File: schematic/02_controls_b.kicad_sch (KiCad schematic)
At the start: 19 parts, among them SW107 F sharp, SW108 G, SW109 G sharp, SW110 A, SW111 A sharp, SW112 B, U402 74HC14

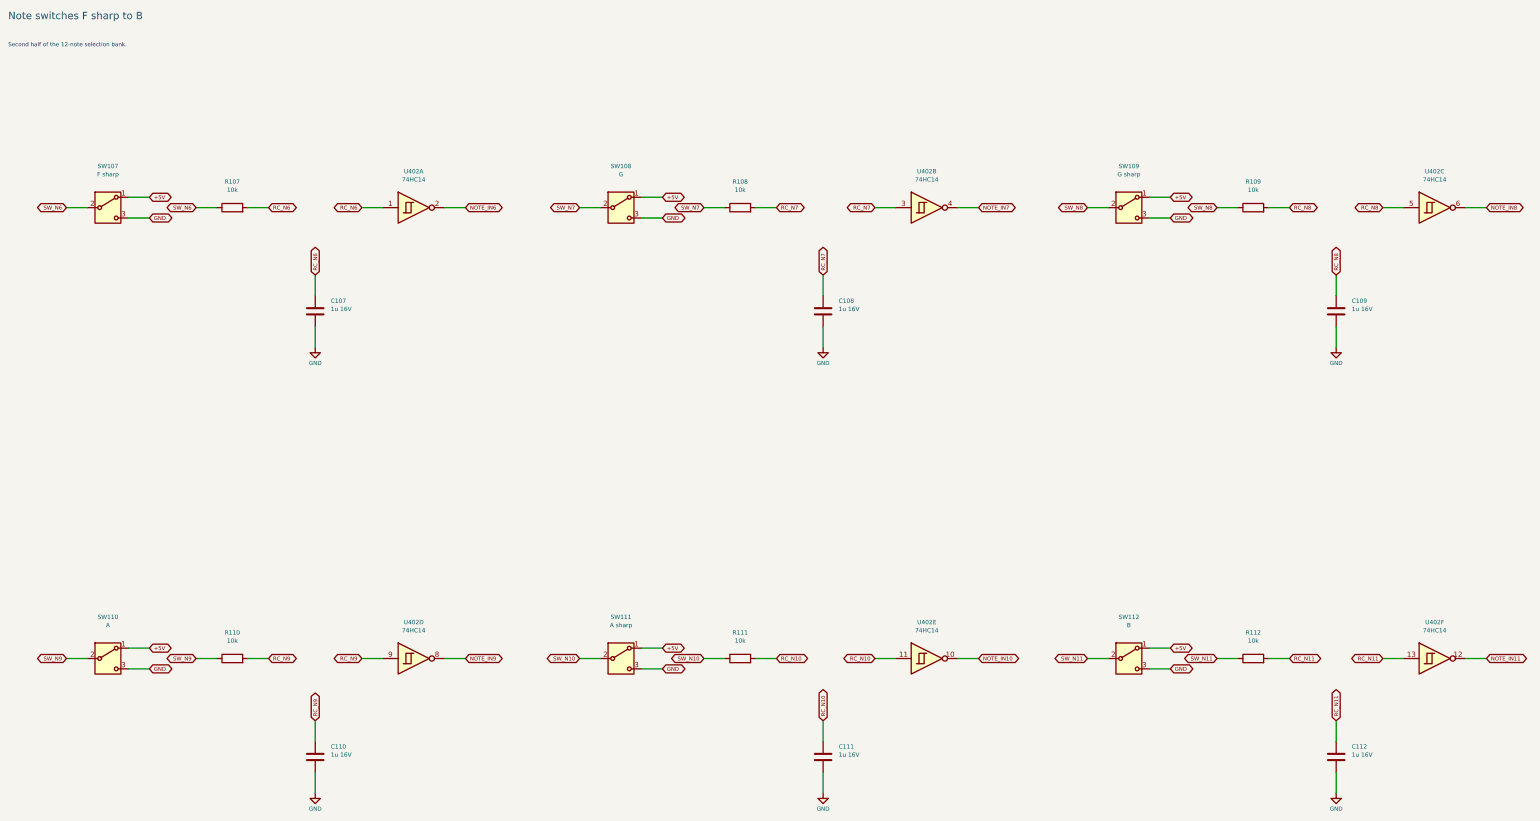
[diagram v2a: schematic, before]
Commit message: pick controls and start pcb placement
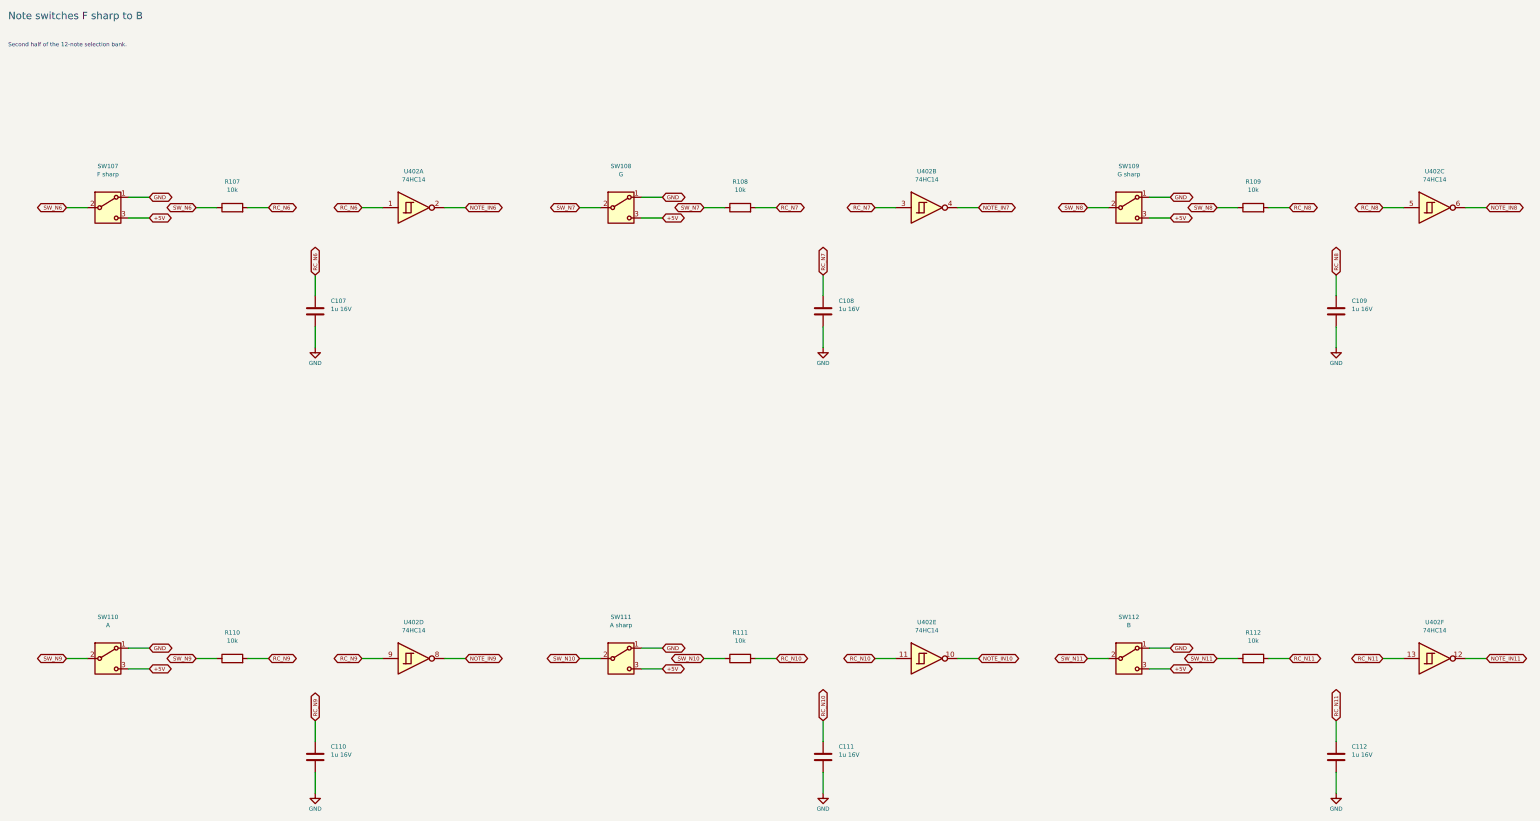
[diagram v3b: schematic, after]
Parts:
- SW107, SW108, SW109, SW110, SW111, SW112: footprint (none) -> Arpeggiator:SW_Dailywell_1M_SPDT_M2; MPN (none) -> 1MS1T1B1M2QES; Manufacturer (none) -> Dailywell; Supplier (none) -> Tayda; Supplier URL (none) -> https://www.taydaelectronics.com/electromechanical/switches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
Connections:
- net +5V: now also SW107.3 (C), SW108.3 (C), SW109.3 (C), SW110.3 (C), SW111.3 (C), SW112.3 (C); no longer SW107.1 (A), SW108.1 (A), SW109.1 (A), SW110.1 (A), SW111.1 (A), SW112.1 (A)
- net GND: now also SW107.1 (A), SW108.1 (A), SW109.1 (A), SW110.1 (A), SW111.1 (A), SW112.1 (A); no longer SW107.3 (C), SW108.3 (C), SW109.3 (C), SW110.3 (C), SW111.3 (C), SW112.3 (C)
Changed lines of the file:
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@@
       )
     )
-    (property "Footprint" ""
+    (property "Footprint" "Arpeggiator:SW_Dailywell_1M_SPDT_M2"
       (at 44.45 54.61 0.0)
       (effects
@@
       )
     )
-    (property "Datasheet" ""
+    (property "Datasheet" "https://www.taydaelectronics.com/datasheets/files/1M_series.pdf"
       (at 44.45 54.61 0.0)
       (effects
         (font
           (size 1.05 1.05)
+        )
+        (hide yes)
+      )
+    )
+    (property "MPN" "1MS1T1B1M2QES"
+      (at 44.45 64.77 0.0)
+      (effects
+        (font
+          (size 1.0 1.0)
+        )
+        (hide yes)
+      )
+    )
+    (property "Manufacturer" "Dailywell"
+      (at 44.45 64.77 0.0)
+      (effects
+        (font
+          (size 1.0 1.0)
+        )
+        (hide yes)
+      )
+    )
+    (property "Supplier" "Tayda"
+      (at 44.45 64.77 0.0)
+      (effects
+        (font
+          (size 1.0 1.0)
+        )
+        (hide yes)
+      )
+    )
+    (property "Supplier URL" "https://www.taydaelectronics.com/electromechanical/switches-key-pad/toggle-switch/mini-toggle-switch-spdt-on-none-on-pc-thru-hole.html"
+      (at 44.45 64.77 0.0)
+      (effects
+        (font
+          (size 1.0 1.0)
         )
         (hide yes)
@@
     )
   )
-  (global_label "+5V"
+  (global_label "GND"
     (shape bidirectional)
     (at 54.61 62.23 0.0)
@@
     )
   )
-  (global_label "GND"
+  (global_label "+5V"
     (shape bidirectional)
     (at 54.61 67.31 0.0)
@@
       )
     )
-    (property "Footprint" ""
+    (property "Footprint" "Arpeggiator:SW_Dailywell_1M_SPDT_M2"
       (at 170.18 54.61 0.0)
       (effects
@@
       )
     )
-    (property "Datasheet" ""
+    (property "Datasheet" "https://www.taydaelectronics.com/datasheets/files/1M_series.pdf"
       (at 170.18 54.61 0.0)
       (effects
         (font
           (size 1.05 1.05)
+        )
+        (hide yes)
+      )
+    )
+    (property "MPN" "1MS1T1B1M2QES"
+      (at 170.18 64.77 0.0)
+      (effects
+        (font
+          (size 1.0 1.0)
+        )
+        (hide yes)
+      )
+    )
+    (property "Manufacturer" "Dailywell"
+      (at 170.18 64.77 0.0)
+      (effects
+        (font
+          (size 1.0 1.0)
+        )
+        (hide yes)
+      )
+    )
+    (property "Supplier" "Tayda"
+      (at 170.18 64.77 0.0)
+      (effects
+        (font
+          (size 1.0 1.0)
+        )
+        (hide yes)
+      )
+    )
+    (property "Supplier URL" "https://www.taydaelectronics.com/electromechanical/switches-key-pad/toggle-switch/mini-toggle-switch-spdt-on-none-on-pc-thru-hole.html"
+      (at 170.18 64.77 0.0)
+      (effects
+        (font
+          (size 1.0 1.0)
         )
         (hide yes)
@@
     )
   )
-  (global_label "+5V"
+  (global_label "GND"
     (shape bidirectional)
     (at 180.34 62.23 0.0)
@@
     )
   )
-  (global_label "GND"
+  (global_label "+5V"
     (shape bidirectional)
     (at 180.34 67.31 0.0)
@@
       )
     )
-    (property "Footprint" ""
+    (property "Footprint" "Arpeggiator:SW_Dailywell_1M_SPDT_M2"
       (at 294.64 54.61 0.0)
       (effects
@@
       )
     )
-    (property "Datasheet" ""
+    (property "Datasheet" "https://www.taydaelectronics.com/datasheets/files/1M_series.pdf"
       (at 294.64 54.61 0.0)
       (effects
         (font
           (size 1.05 1.05)
+        )
+        (hide yes)
+      )
+    )
+    (property "MPN" "1MS1T1B1M2QES"
+      (at 294.64 64.77 0.0)
+      (effects
+        (font
+          (size 1.0 1.0)
+        )
+        (hide yes)
+      )
+    )
+    (property "Manufacturer" "Dailywell"
+      (at 294.64 64.77 0.0)
+      (effects
+        (font
+          (size 1.0 1.0)
+        )
+        (hide yes)
+      )
+    )
+    (property "Supplier" "Tayda"
+      (at 294.64 64.77 0.0)
+      (effects
+        (font
+          (size 1.0 1.0)
+        )
+        (hide yes)
+      )
+    )
+    (property "Supplier URL" "https://www.taydaelectronics.com/electromechanical/switches-key-pad/toggle-switch/mini-toggle-switch-spdt-on-none-on-pc-thru-hole.html"
+      (at 294.64 64.77 0.0)
+      (effects
+        (font
+          (size 1.0 1.0)
         )
         (hide yes)
@@
     )
   )
-  (global_label "+5V"
+  (global_label "GND"
     (shape bidirectional)
     (at 304.8 62.23 0.0)
@@
     )
   )
-  (global_label "GND"
+  (global_label "+5V"
     (shape bidirectional)
     (at 304.8 67.31 0.0)
@@
       )
     )
-    (property "Footprint" ""
+    (property "Footprint" "Arpeggiator:SW_Dailywell_1M_SPDT_M2"
       (at 44.45 165.1 0.0)
       (effects
@@
       )
     )
-    (property "Datasheet" ""
+    (property "Datasheet" "https://www.taydaelectronics.com/datasheets/files/1M_series.pdf"
       (at 44.45 165.1 0.0)
       (effects
         (font
           (size 1.05 1.05)
+        )
+        (hide yes)
+      )
+    )
+    (property "MPN" "1MS1T1B1M2QES"
+      (at 44.45 175.26 0.0)
+      (effects
+        (font
+          (size 1.0 1.0)
+        )
+        (hide yes)
+      )
+    )
+    (property "Manufacturer" "Dailywell"
+      (at 44.45 175.26 0.0)
+      (effects
+        (font
+          (size 1.0 1.0)
+        )
+        (hide yes)
+      )
+    )
+    (property "Supplier" "Tayda"
+      (at 44.45 175.26 0.0)
+      (effects
+        (font
+          (size 1.0 1.0)
+        )
+        (hide yes)
+      )
+    )
+    (property "Supplier URL" "https://www.taydaelectronics.com/electromechanical/switches-key-pad/toggle-switch/mini-toggle-switch-spdt-on-none-on-pc-thru-hole.html"
+      (at 44.45 175.26 0.0)
+      (effects
+        (font
+          (size 1.0 1.0)
         )
         (hide yes)
@@
     )
   )
-  (global_label "+5V"
+  (global_label "GND"
     (shape bidirectional)
     (at 54.61 172.72 0.0)
@@
     )
   )
-  (global_label "GND"
+  (global_label "+5V"
     (shape bidirectional)
     (at 54.61 177.8 0.0)
@@
       )
     )
-    (property "Footprint" ""
+    (property "Footprint" "Arpeggiator:SW_Dailywell_1M_SPDT_M2"
       (at 170.18 165.1 0.0)
       (effects
@@
       )
     )
-    (property "Datasheet" ""
+    (property "Datasheet" "https://www.taydaelectronics.com/datasheets/files/1M_series.pdf"
       (at 170.18 165.1 0.0)
       (effects
         (font
           (size 1.05 1.05)
+        )
+        (hide yes)
+      )
+    )
+    (property "MPN" "1MS1T1B1M2QES"
+      (at 170.18 175.26 0.0)
+      (effects
+        (font
+          (size 1.0 1.0)
+        )
+        (hide yes)
+      )
+    )
+    (property "Manufacturer" "Dailywell"
+      (at 170.18 175.26 0.0)
+      (effects
+        (font
+          (size 1.0 1.0)
+        )
+        (hide yes)
+      )
+    )
+    (property "Supplier" "Tayda"
+      (at 170.18 175.26 0.0)
+      (effects
+        (font
+          (size 1.0 1.0)
+        )
+        (hide yes)
+      )
+    )
+    (property "Supplier URL" "https://www.taydaelectronics.com/electromechanical/switches-key-pad/toggle-switch/mini-toggle-switch-spdt-on-none-on-pc-thru-hole.html"
+      (at 170.18 175.26 0.0)
+      (effects
+        (font
+          (size 1.0 1.0)
         )
         (hide yes)
@@
     )
   )
-  (global_label "+5V"
+  (global_label "GND"
     (shape bidirectional)
     (at 180.34 172.72 0.0)
@@
     )
   )
-  (global_label "GND"
+  (global_label "+5V"
     (shape bidirectional)
     (at 180.34 177.8 0.0)
@@
       )
     )
-    (property "Footprint" ""
+    (property "Footprint" "Arpeggiator:SW_Dailywell_1M_SPDT_M2"
       (at 294.64 165.1 0.0)
       (effects
@@
       )
     )
-    (property "Datasheet" ""
+    (property "Datasheet" "https://www.taydaelectronics.com/datasheets/files/1M_series.pdf"
       (at 294.64 165.1 0.0)
       (effects
         (font
           (size 1.05 1.05)
+        )
+        (hide yes)
+      )
+    )
+    (property "MPN" "1MS1T1B1M2QES"
+      (at 294.64 175.26 0.0)
+      (effects
+        (font
+          (size 1.0 1.0)
+        )
+        (hide yes)
+      )
+    )
+    (property "Manufacturer" "Dailywell"
+      (at 294.64 175.26 0.0)
+      (effects
+        (font
+          (size 1.0 1.0)
+        )
+        (hide yes)
+      )
+    )
+    (property "Supplier" "Tayda"
+      (at 294.64 175.26 0.0)
+      (effects
+        (font
+          (size 1.0 1.0)
+        )
+        (hide yes)
+      )
+    )
+    (property "Supplier URL" "https://www.taydaelectronics.com/electromechanical/switches-key-pad/toggle-switch/mini-toggle-switch-spdt-on-none-on-pc-thru-hole.html"
+      (at 294.64 175.26 0.0)
+      (effects
+        (font
+          (size 1.0 1.0)
         )
         (hide yes)
@@
     )
   )
-  (global_label "+5V"
+  (global_label "GND"
     (shape bidirectional)
     (at 304.8 172.72 0.0)
@@
     )
   )
-  (global_label "GND"
+  (global_label "+5V"
     (shape bidirectional)
     (at 304.8 177.8 0.0)
